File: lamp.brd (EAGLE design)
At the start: 184.2 x 38.1 mm, 63 parts, among them P1 10kΩ, P2 2MΩ

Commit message: Moved pfet f2 so it's not sitting on the back of an LED
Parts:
- moved F2 7.62 mm to (13.9, 9.91)
- moved C5 7.62 mm to (17.5, 9.91)
- moved R13 7.62 mm to (17.5, 5.08)
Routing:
- net +12V: track 11.2 -> 13.0 mm
- net N$45: track 213.5 -> 215.0 mm
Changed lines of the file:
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@@
 <grid distance="0.1" unitdist="inch" unit="inch" style="lines" multiple="1" display="no" altdistance="0.01" altunitdist="inch" altunit="inch"/>
 <layers>
-<layer number="1" name="Top" color="4" fill="1" visible="yes" active="yes"/>
+<layer number="1" name="Top" color="4" fill="1" visible="no" active="yes"/>
 <layer number="16" name="Bottom" color="1" fill="1" visible="yes" active="yes"/>
 <layer number="17" name="Pads" color="2" fill="1" visible="yes" active="yes"/>
@@
 <text x="92.075" y="20.828" size="1.778" layer="26" rot="MR180" align="top-center">UC</text>
 <text x="91.059" y="8.128" size="1.778" layer="26" rot="MR0" align="top-center">VR</text>
-<text x="4.064" y="10.0236" size="1.778" layer="26" rot="MR90" align="top-center">F2</text>
+<text x="11.684" y="10.0236" size="1.778" layer="26" rot="MR90" align="top-center">F2</text>
 <text x="70.231" y="15.24" size="1.778" layer="26" rot="MR0" align="top-center">P2</text>
 <text x="77.089" y="13.208" size="1.778" layer="26" rot="MR0" align="top-center">C4</text>
@@
 <rectangle x1="96.2025" y1="16.1925" x2="101.2825" y2="18.7325" layer="1"/>
 <rectangle x1="96.2025" y1="19.3675" x2="101.2825" y2="21.9075" layer="1"/>
-<text x="11.176" y="9.906" size="1.778" layer="26" rot="MR270" align="top-center">C5</text>
-<text x="11.176" y="5.08" size="1.778" layer="26" rot="MR270" align="top-center">R13</text>
+<text x="18.796" y="9.906" size="1.778" layer="26" rot="MR270" align="top-center">C5</text>
+<text x="18.796" y="5.08" size="1.778" layer="26" rot="MR270" align="top-center">R13</text>
 <text x="7.112" y="24.638" size="1.778" layer="26" rot="MR0">J1</text>
 <text x="92.075" y="28.956" size="1.778" layer="26" rot="MR0" align="bottom-center">F1</text>
@@
 </element>
 <element name="C3" library=" Barebones-Arduino" package="0805" value="10nF" x="87.249" y="10.668" rot="MR270"/>
-<element name="F2" library="lamp" package="SOT-23-3" value="SI2319DS" x="6.2992" y="9.906" smashed="yes" rot="MR0"/>
+<element name="F2" library="lamp" package="SOT-23-3" value="SI2319DS" x="13.9192" y="9.906" smashed="yes" rot="MR0"/>
 <element name="U$32" library="lamp" package="SM4" value="HEADER-3X1" x="7.62" y="19.05" rot="MR270"/>
 <element name="P1" library="lamp" package="3361P" value="10kΩ" x="113.919" y="19.05" smashed="yes" rot="MR270"/>
@@
 <element name="P2" library="lamp" package="3361P" value="2MΩ" x="70.231" y="19.05" smashed="yes" rot="MR90"/>
 <element name="C4" library=" Barebones-Arduino" package="0805" value="100pF" x="77.216" y="15.621" rot="MR270"/>
-<element name="R13" library=" Barebones-Arduino" package="0805" value="100kΩ" x="9.906" y="5.08" rot="MR90"/>
-<element name="C5" library=" Barebones-Arduino" package="0805" value="1µF" x="9.906" y="9.906" rot="MR270"/>
+<element name="R13" library=" Barebones-Arduino" package="0805" value="100kΩ" x="17.526" y="5.08" rot="MR90"/>
+<element name="C5" library=" Barebones-Arduino" package="0805" value="1µF" x="17.526" y="9.906" rot="MR270"/>
 <element name="F1" library="lamp" package="SOT-23-3" value="SI2318DS" x="92.075" y="27.178" smashed="yes" rot="MR90"/>
 </elements>
@@
 <wire x1="64.4525" y1="1.524" x2="83.5025" y2="1.524" width="0.6096" layer="1"/>
 <wire x1="83.5025" y1="1.524" x2="92.075" y2="1.524" width="0.6096" layer="1"/>
-<wire x1="92.075" y1="1.524" x2="101.6" y2="1.524" width="0.6096" layer="1"/>
+<wire x1="92.075" y1="1.524" x2="102.5525" y2="1.524" width="0.6096" layer="1"/>
 <wire x1="102.5525" y1="1.524" x2="121.6025" y2="1.524" width="0.6096" layer="1"/>
 <wire x1="121.6025" y1="1.524" x2="140.6525" y2="1.524" width="0.6096" layer="1"/>
@@
 <wire x1="26.3525" y1="3.4925" x2="26.3525" y2="1.524" width="0.6096" layer="1"/>
 <via x="7.366" y="1.524" extent="1-16" drill="0.5"/>
-<wire x1="5.3492" y1="8.756" x2="5.3492" y2="3.5408" width="0.6096" layer="16"/>
-<wire x1="5.3492" y1="3.5408" x2="7.366" y2="1.524" width="0.6096" layer="16"/>
 <via x="92.075" y="1.524" extent="1-16" drill="0.5"/>
 <wire x1="92.075" y1="1.524" x2="92.075" y2="6.35" width="0.3048" layer="16"/>
@@
 <wire x1="121.6025" y1="3.4925" x2="121.6025" y2="1.524" width="0.6096" layer="1"/>
 <wire x1="102.5525" y1="3.4925" x2="102.5525" y2="1.524" width="0.6096" layer="1"/>
-<wire x1="102.5525" y1="1.524" x2="101.6" y2="1.524" width="0.6096" layer="1"/>
+<wire x1="12.9692" y1="8.756" x2="7.366" y2="3.1528" width="0.6096" layer="16"/>
+<wire x1="7.366" y1="3.1528" x2="7.366" y2="1.524" width="0.6096" layer="16"/>
 </signal>
 <signal name="N$50">
@@
 <contactref element="R13" pad="2"/>
 <contactref element="C5" pad="2"/>
-<wire x1="9.906" y1="5.93" x2="9.906" y2="9.056" width="0.6096" layer="16"/>
-<wire x1="9.906" y1="9.056" x2="7.5492" y2="9.056" width="0.6096" layer="16"/>
-<wire x1="7.5492" y1="9.056" x2="7.2492" y2="8.756" width="0.6096" layer="16"/>
+<wire x1="17.526" y1="5.93" x2="17.526" y2="9.056" width="0.6096" layer="16"/>
+<wire x1="17.526" y1="9.056" x2="15.1692" y2="9.056" width="0.6096" layer="16"/>
+<wire x1="15.1692" y1="9.056" x2="14.8692" y2="8.756" width="0.6096" layer="16"/>
 </signal>
 <signal name="N$33">
@@
 <contactref element="F2" pad="P$3"/>
 <contactref element="U$32" pad="P$1"/>
-<wire x1="9.906" y1="10.756" x2="6.3242" y2="10.756" width="0.6096" layer="16"/>
-<wire x1="6.3242" y1="10.756" x2="6.2992" y2="10.781" width="0.6096" layer="16"/>
-<wire x1="9.37" y1="17.05" x2="9.37" y2="13.8518" width="0.6096" layer="16"/>
-<wire x1="9.37" y1="13.8518" x2="6.2992" y2="10.781" width="0.6096" layer="16"/>
+<wire x1="17.526" y1="10.756" x2="13.9442" y2="10.756" width="0.6096" layer="16"/>
+<wire x1="13.9442" y1="10.756" x2="13.9192" y2="10.781" width="0.6096" layer="16"/>
+<wire x1="9.37" y1="17.05" x2="9.37" y2="13.236" width="0.6096" layer="16"/>
+<wire x1="9.37" y1="13.236" x2="11.825" y2="10.781" width="0.6096" layer="16"/>
+<wire x1="11.825" y1="10.781" x2="13.9192" y2="10.781" width="0.6096" layer="16"/>
 </signal>
 <signal name="N$17">

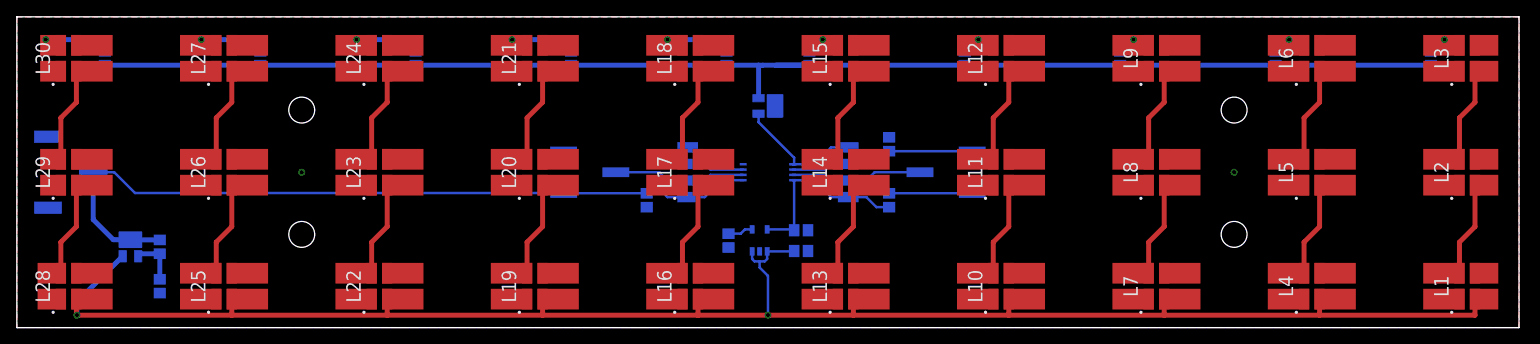
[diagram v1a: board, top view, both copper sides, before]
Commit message: Pulled the supply rail for the LED banks onto the back of the board.
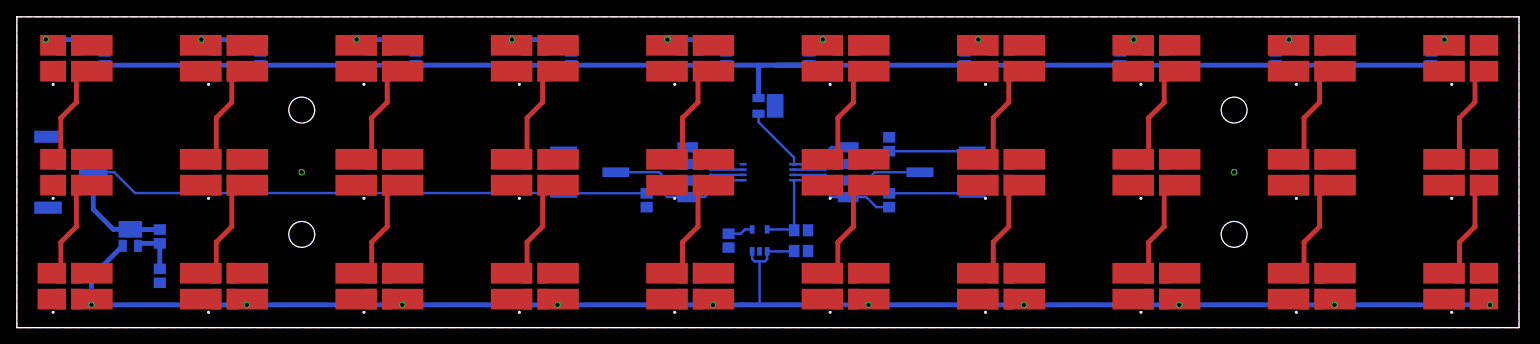
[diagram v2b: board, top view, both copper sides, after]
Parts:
- moved C5 1.27 mm to (17.5, 11.2)
- moved F2 1.27 mm to (13.9, 11.2)
- moved R13 1.27 mm to (17.5, 6.35)
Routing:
- net N$45: track 215.0 -> 220.5 mm, vias 2 -> 10
- net +12V: track 13.0 -> 11.7 mm
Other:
- board text removed: "L1"
- board text removed: "L10"
- board text removed: "L11"
- board text removed: "L12"
- board text removed: "L13"
- board text removed: "L14"
- board text removed: "L15"
- board text removed: "L16"
- board text removed: "L17"
- board text removed: "L18"
- board text removed: "L19"
- board text removed: "L2"
- board text removed: "L20"
- board text removed: "L21"
- board text removed: "L22"
- board text removed: "L23"
- board text removed: "L24"
- board text removed: "L25"
- board text removed: "L26"
- board text removed: "L27"
- board text removed: "L28"
- board text removed: "L29"
- board text removed: "L3"
- board text removed: "L30"
- board text removed: "L4"
- board text removed: "L5"
- board text removed: "L6"
- board text removed: "L7"
- board text removed: "L8"
- board text removed: "L9"

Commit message: Added fancy silk screen on front of board for Art Reasons.
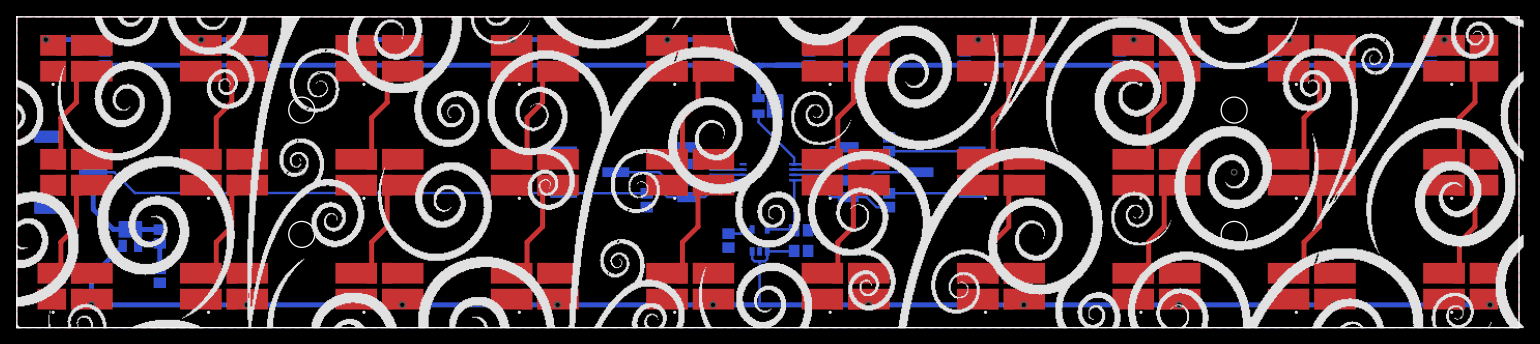
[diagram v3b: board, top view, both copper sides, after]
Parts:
- R13: value 100kΩ -> 10kΩ
